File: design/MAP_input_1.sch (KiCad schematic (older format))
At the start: 6 parts, among them U6 MPX4250A

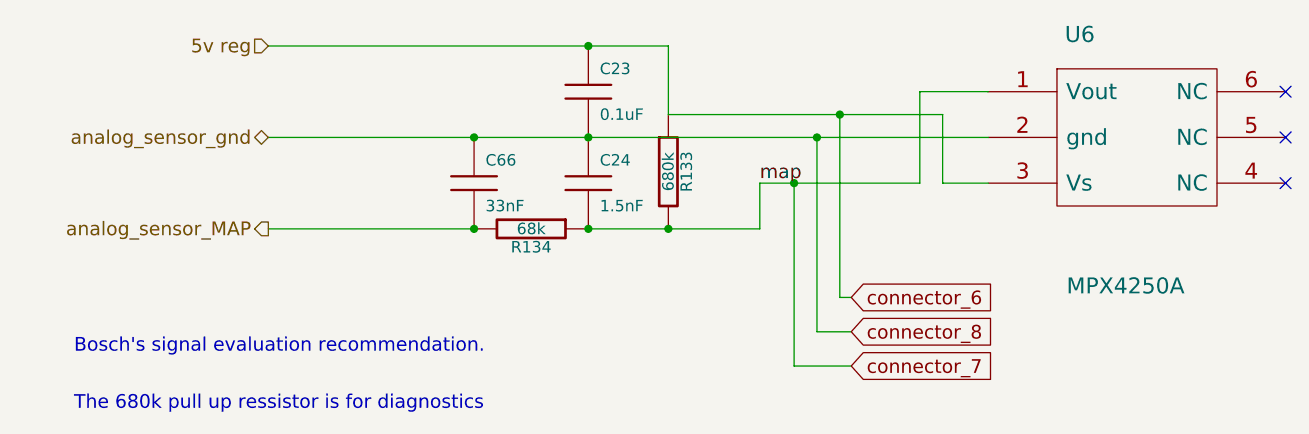
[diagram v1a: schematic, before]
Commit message: Schematic BOM is now fully populated with only 3 exceptions, .cmp file is obsolete at this point, so it has been removed.
Signed-off-by: Jared Harvey <TortiseGIT@jaredharvey.com>
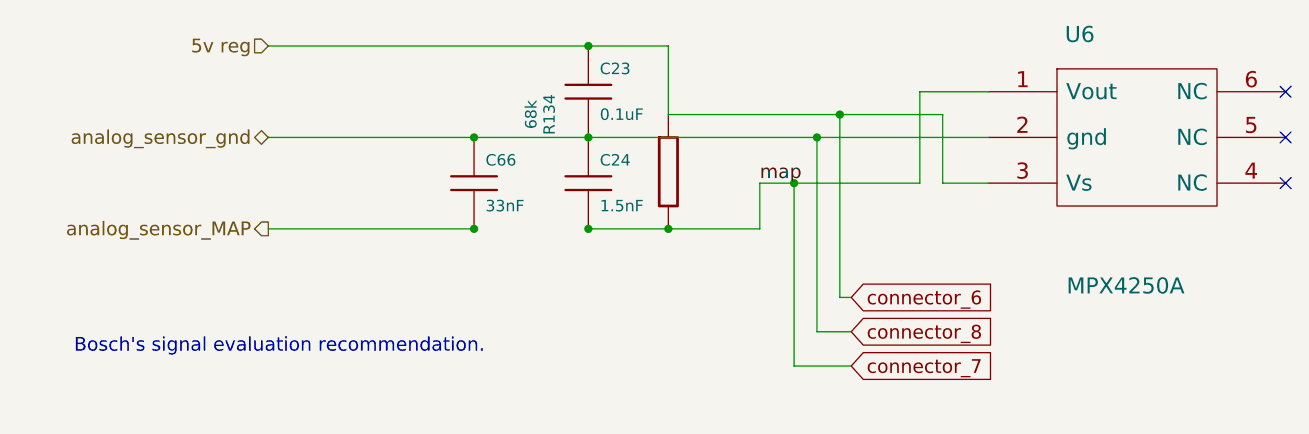
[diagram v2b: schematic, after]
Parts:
- removed R133: 680k, symbol R
- R134: footprint (none) -> SM0805; Field2 RMCF0805JT68K0CT-ND -> (none); Power (none) -> .125w; construct (none) -> metal oxide; mfg (none) -> Panasonic-ECG; mfg# (none) -> ERJ-6GEYJ684V; misc (none) -> other,more,stuff; tolerance (none) -> 5%; vend1 (none) -> digikey; vend1# (none) -> P680KACT-ND
- U6: footprint SOP_case_482 -> SIL-6; Field1 newark,75C3857 -> (none); Field2 MPX4250AP-ND -> (none); Field3 vendor2, thru w hem -> (none); Field4 vendor2, smd w hem -> (none); mfg (none) -> freescale; mfg# (none) -> MPX4250AP; vend1 (none) -> digikey; vend1# (none) -> MPX4250AP-ND
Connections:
- net analog_sensor_MAP: no longer R134.2
- net connector_6: now also R134.1
- net connector_7: now also R134.2; no longer R134.1
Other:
- note removed: "The 680k pull up ressistor is for diagnostics"
- moved on the sheet: R134
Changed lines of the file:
@@
-EESchema Schematic File Version 2  date 2/16/2011 5:39:17 AM
+EESchema Schematic File Version 2  date 2/16/2011 8:44:20 AM
 LIBS:power
 LIBS:freeEMS_lib
@@
 F 0 "U6" H 5950 2250 70  0000 C CNN
 F 1 "MPX4250A" H 6150 1150 70  0000 C CNN
-F 2 "SOP_case_482" V 2230 2800 60  0001 C CNN
-F 4 "newark,75C3857" V 2230 2800 60  0001 C CNN "Field1"
-F 5 "MPX4250AP-ND" V 2230 2800 60  0001 C CNN "Field2"
-F 6 "vendor2, thru w hem" V 2230 2800 60  0001 C CNN "Field3"
-F 7 "vendor2, smd w hem" V 2230 2800 60  0001 C CNN "Field4"
+F 2 "SIL-6" V 2230 2800 60  0001 C CNN
+F 4 "freescale" V 2230 2800 60  0001 C CNN "mfg"
+F 5 "MPX4250AP" V 2230 2800 60  0001 C CNN "mfg#"
+F 6 "digikey" V 2230 2800 60  0001 C CNN "vend1"
+F 7 "MPX4250AP-ND" V 2230 2800 60  0001 C CNN "vend1#"
 F 8 "x,x" V 2230 2800 60  0001 C CNN "Field5"
 F 9 "x,x" V 2230 2800 60  0001 C CNN "Field6"
@@
 L R R134
 U 1 1 4C4AEFA3
-P 3550 2000
+P 4150 1750
 F 0 "R134" V 3630 2000 50  0000 C CNN
 F 1 "68k" V 3550 2000 50  0000 C CNN
-F 5 "RMCF0805JT68K0CT-ND" H 3550 2000 60  0001 C CNN "Field2"
-	1    3550 2000
-	0    1    1    0
-$EndComp
-Text Notes 1550 2800 0    60   ~ 0
-The 680k pull up ressistor is for diagnostics
-$Comp
-L R R133
-U 1 1 4C4AEDC5
-P 4150 1750
-F 0 "R133" V 4230 1750 50  0000 C CNN
-F 1 "680k" V 4150 1750 50  0000 C CNN
+F 2 "SM0805" V 1130 2600 60  0001 C CNN
 F 4 "Panasonic-ECG" V 2380 2650 60  0001 C CNN "mfg"
 F 5 "ERJ-6GEYJ684V" V 2380 2650 60  0001 C CNN "mfg#"

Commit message: updated AAP and MAP footprints
Signed-off-by: Jared Harvey <TortiseGIT@jaredharvey.com>
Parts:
- U6: footprint SIL-6 -> MPX4---AP
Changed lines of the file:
@@
-EESchema Schematic File Version 2  date 2/17/2011 8:28:50 AM
+EESchema Schematic File Version 2  date 2/20/2011 12:36:48 PM
 LIBS:power
 LIBS:freeEMS_lib
@@
 Sheet 44 56
 Title "Puma board"
-Date "17 feb 2011"
+Date "20 feb 2011"
 Rev "v0.02"
 Comp "diyefi.org"
@@
 F 0 "U6" H 5950 2250 70  0000 C CNN
 F 1 "MPX4250A" H 6150 1150 70  0000 C CNN
-F 2 "SIL-6" V 2230 2800 60  0001 C CNN
+F 2 "MPX4---AP" V 2230 2800 60  0001 C CNN
 F 4 "freescale" V 2230 2800 60  0001 C CNN "mfg"
 F 5 "MPX4250AP" V 2230 2800 60  0001 C CNN "mfg#"
